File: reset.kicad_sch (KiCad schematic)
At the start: 12 parts

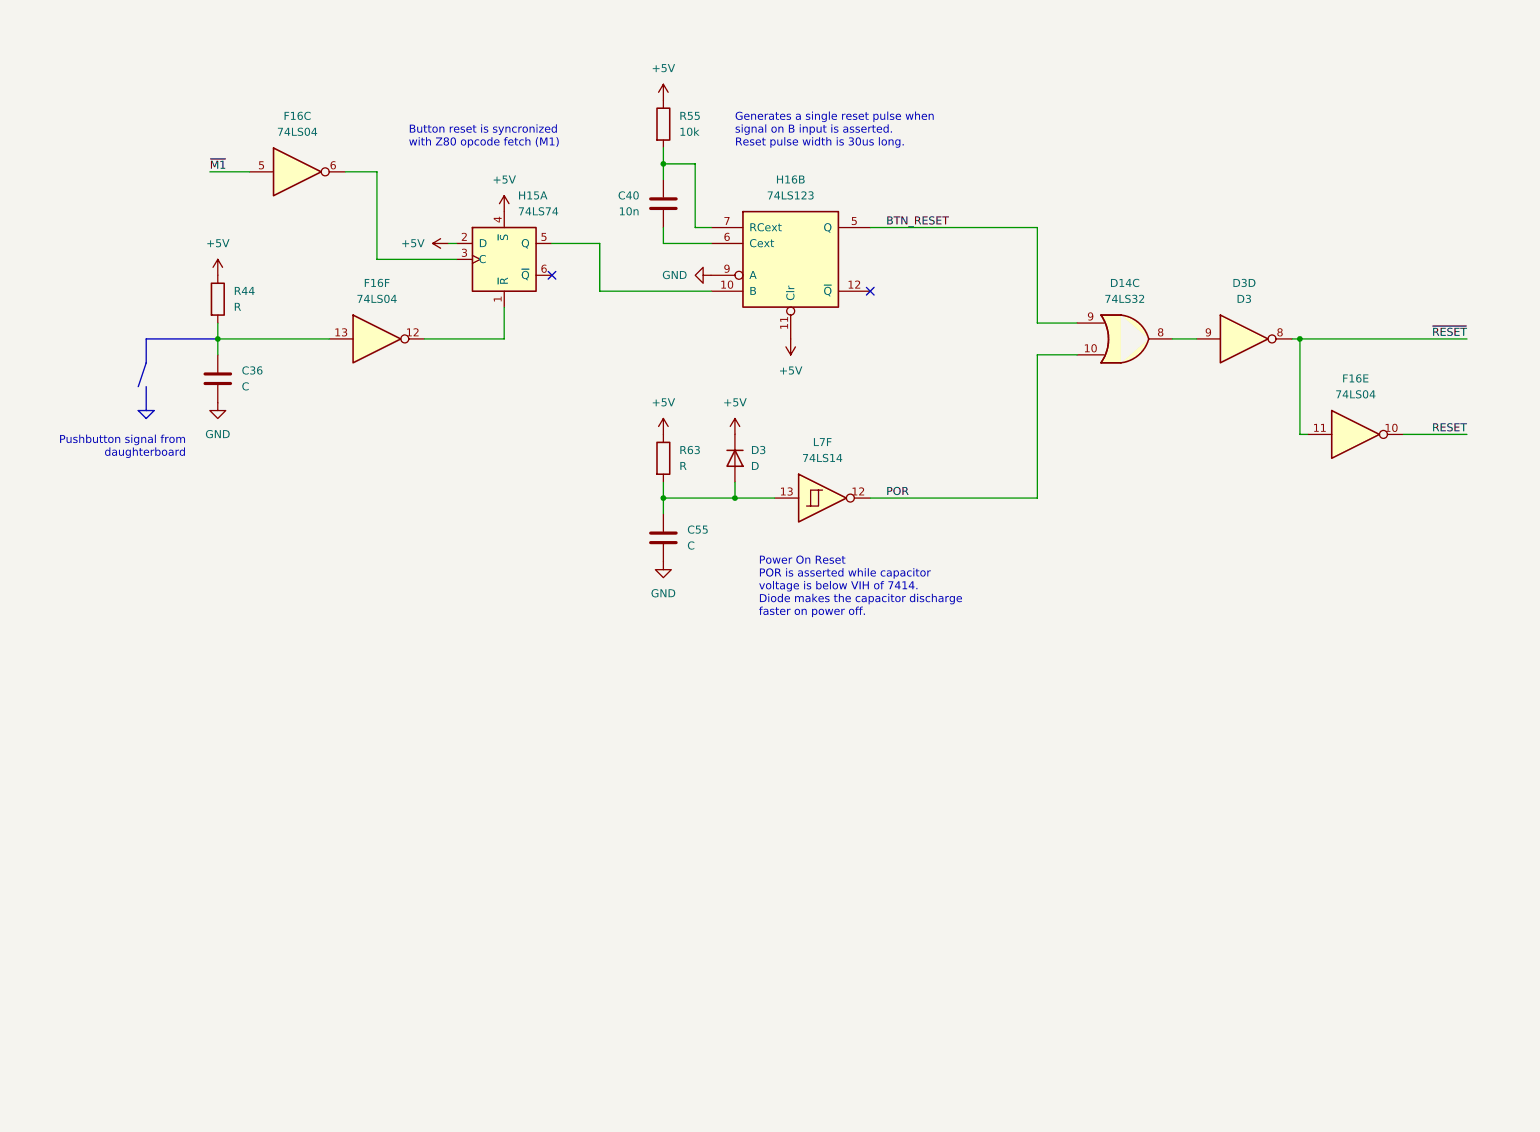
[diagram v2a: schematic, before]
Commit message: Moved clock circuit in the clock/reset sheet
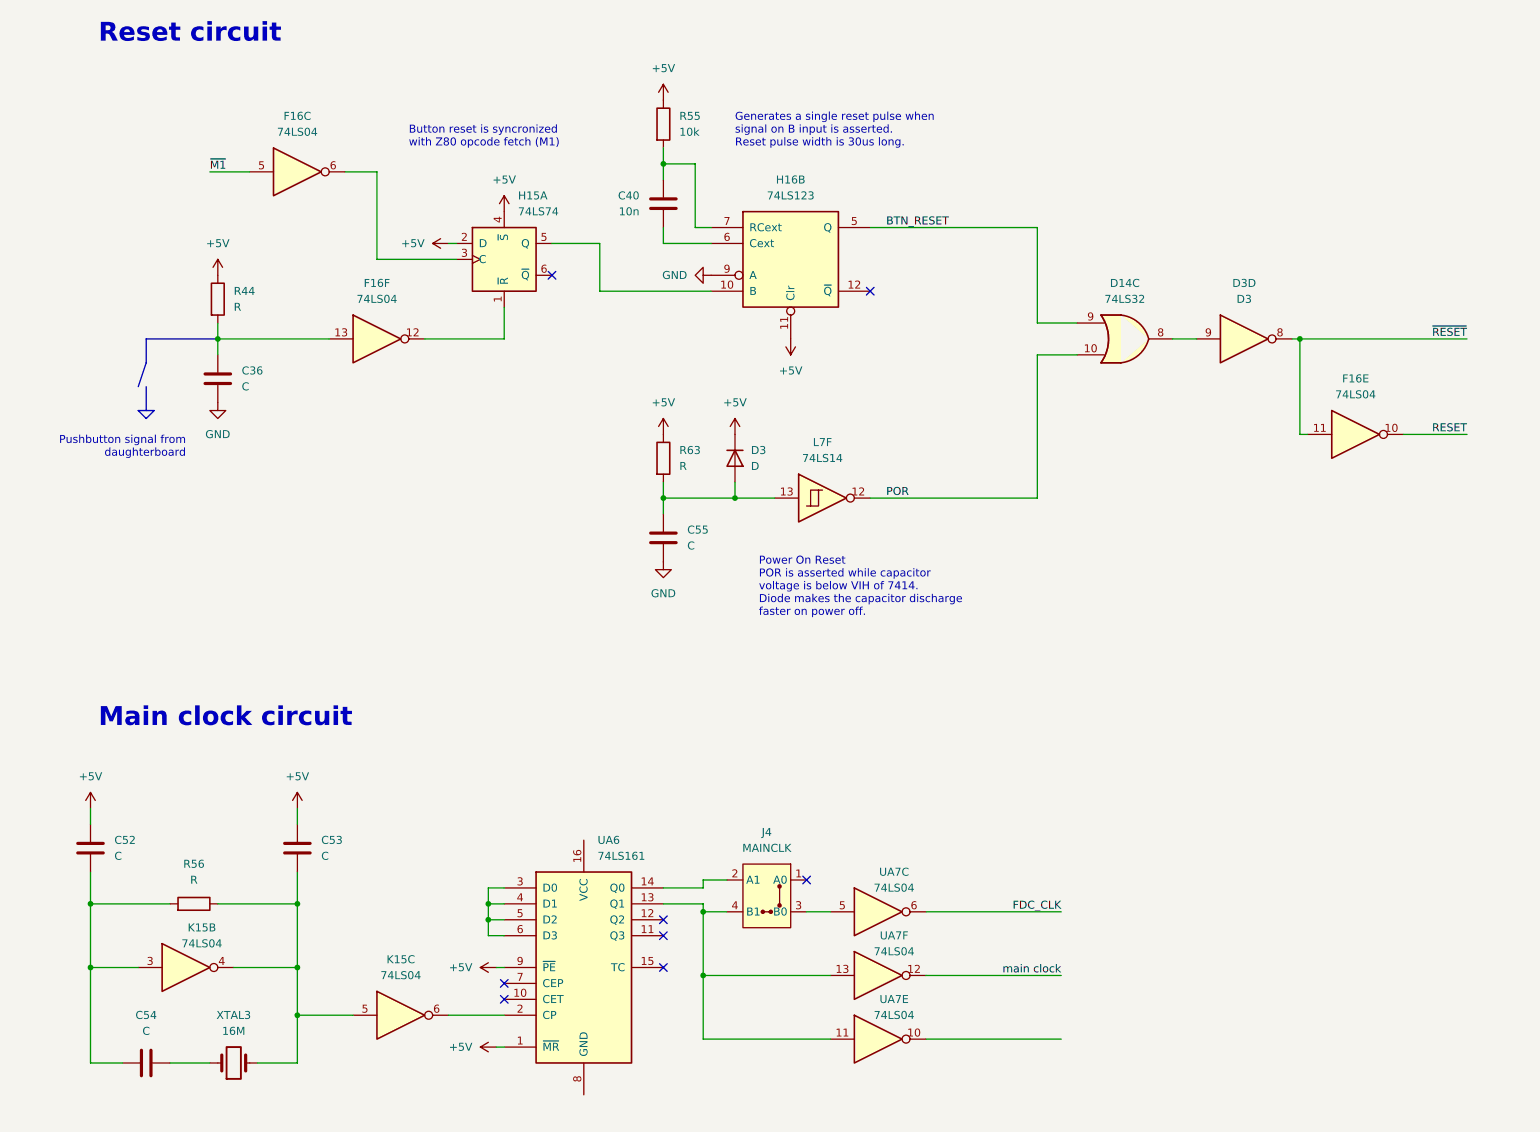
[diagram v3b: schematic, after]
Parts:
- added C52, C53, C54: C, symbol Device:C
- added J4: MAINCLK, symbol ceda:MAINCLK
- added K15, UA7: 74LS04, symbol 74xx:74LS04
- added R56: R, symbol Device:R
- added UA6: 74LS161, symbol 74xx:74LS161
- added XTAL3: 16M, symbol Device:Crystal
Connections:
- net +5V: now also C52.2, C53.2, UA6.1 (~{MR}), UA6.9 (~{PE})
- new net: J4.4 (B1), UA6.13 (Q1), UA7.11, UA7.13
- new net: J4.2 (A1), UA6.14 (Q0)
- new net: K15.6, UA6.2 (CP)
- new net: UA6.3 (D0), UA6.4 (D1), UA6.5 (D2), UA6.6 (D3)
- new net: C52.1, C54.2, K15.3, R56.2
- new net: J4.3 (B0), UA7.5
- new net: C54.1, XTAL3.1
- new net: C53.1, K15.4, K15.5, R56.1, XTAL3.2
- new net FDC_CLK: UA7.6
- new net main clock: UA7.12
- no-connect marks 2 -> 8
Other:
- note added: "Main clock circuit"
- note added: "Reset circuit"

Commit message: Z80 and reset/clock: wire naming
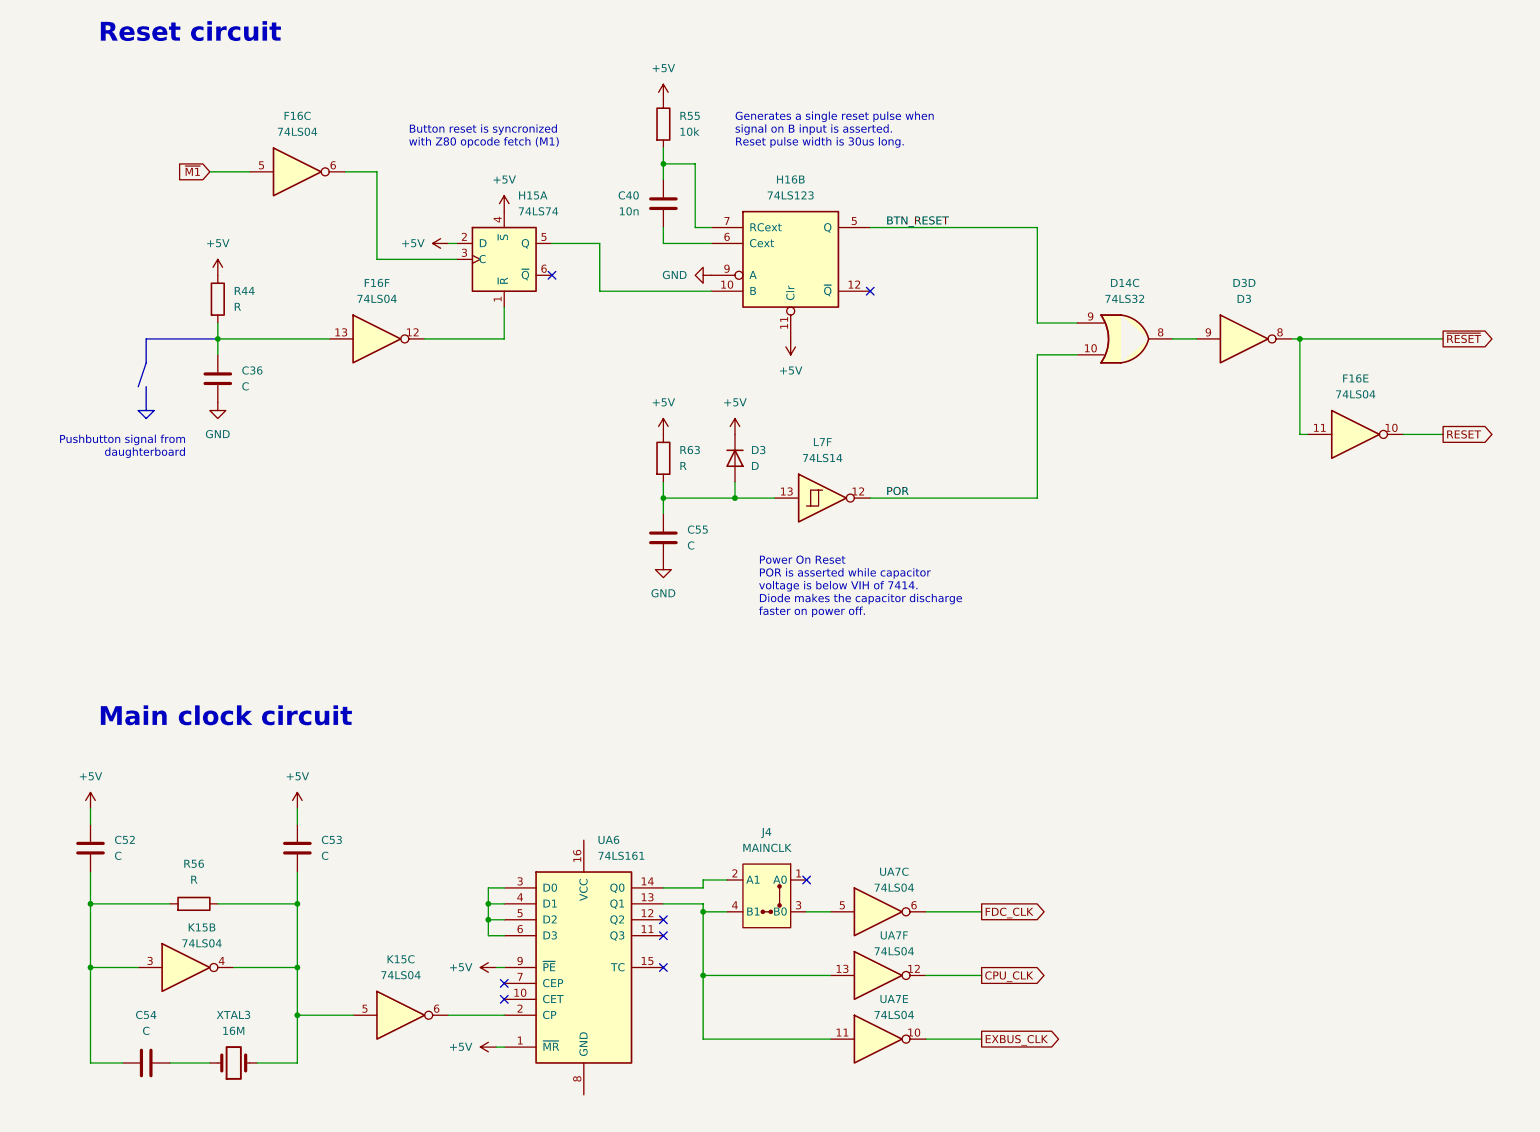
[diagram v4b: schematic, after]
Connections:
- net EXBUS_CLK: now reaches UA7.10
- net main clock renamed CPU_CLK
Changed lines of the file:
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@@
     (stroke (width 0) (type default))
   )
-  (wire (pts (xy 153.67 173.99) (xy 175.26 173.99))
+  (wire (pts (xy 153.67 173.99) (xy 162.56 173.99))
     (stroke (width 0) (type default))
   )
@@
     (stroke (width 0) (type default))
   )
-  (wire (pts (xy 213.36 72.39) (xy 240.03 72.39))
+  (wire (pts (xy 213.36 72.39) (xy 236.22 72.39))
     (stroke (width 0) (type default))
   )
@@
     (stroke (width 0) (type default))
   )
-  (wire (pts (xy 153.67 184.15) (xy 175.26 184.15))
+  (wire (pts (xy 153.67 184.15) (xy 162.56 184.15))
     (stroke (width 0) (type default))
   )
@@
     (stroke (width 0) (type default))
   )
-  (wire (pts (xy 229.87 87.63) (xy 240.03 87.63))
+  (wire (pts (xy 229.87 87.63) (xy 236.22 87.63))
     (stroke (width 0) (type default))
   )
@@
     (stroke (width 0) (type default))
   )
-  (wire (pts (xy 175.26 163.83) (xy 153.67 163.83))
+  (wire (pts (xy 162.56 163.83) (xy 153.67 163.83))
     (stroke (width 0) (type default))
   )
@@
     (effects (font (size 3 3) (thickness 1) bold) (justify left bottom))
   )
-  (label "RESET" (at 240.03 87.63 180) (fields_autoplaced)
-    (effects (font (size 1.27 1.27)) (justify right bottom))
-  )
   (label "BTN_RESET" (at 147.32 54.61 0) (fields_autoplaced)
     (effects (font (size 1.27 1.27)) (justify left bottom))
   )
-  (label "~{RESET}" (at 240.03 72.39 180) (fields_autoplaced)
-    (effects (font (size 1.27 1.27)) (justify right bottom))
-  )
-  (label "~{M1}" (at 39.37 45.72 0) (fields_autoplaced)
-    (effects (font (size 1.27 1.27)) (justify left bottom))
-  )
   (label "POR" (at 147.32 97.79 0) (fields_autoplaced)
     (effects (font (size 1.27 1.27)) (justify left bottom))
   )
-  (label "FDC_CLK" (at 175.26 163.83 180) (fields_autoplaced)
-    (effects (font (size 1.27 1.27)) (justify right bottom))
-  )
-  (label "main clock" (at 175.26 173.99 180) (fields_autoplaced)
-    (effects (font (size 1.27 1.27)) (justify right bottom))
+  (global_label "RESET" (shape output) (at 236.22 87.63 0) (fields_autoplaced)
+    (effects (font (size 1.27 1.27)) (justify left))
+    (property "Intersheetrefs" "${INTERSHEET_REFS}" (at 244.9503 87.63 0)
+      (effects (font (size 1.27 1.27)) (justify left) hide)
+    )
+  )
+  (global_label "CPU_CLK" (shape output) (at 162.56 173.99 0) (fields_autoplaced)
+    (effects (font (size 1.27 1.27)) (justify left))
+    (property "Intersheetrefs" "${INTERSHEET_REFS}" (at 173.9514 173.99 0)
+      (effects (font (size 1.27 1.27)) (justify left) hide)
+    )
+  )
+  (global_label "~{M1}" (shape input) (at 39.37 45.72 180) (fields_autoplaced)
+    (effects (font (size 1.27 1.27)) (justify right))
+    (property "Intersheetrefs" "${INTERSHEET_REFS}" (at 33.7239 45.72 0)
+      (effects (font (size 1.27 1.27)) (justify right) hide)
+    )
+  )
+  (global_label "FDC_CLK" (shape output) (at 162.56 163.83 0) (fields_autoplaced)
+    (effects (font (size 1.27 1.27)) (justify left))
+    (property "Intersheetrefs" "${INTERSHEET_REFS}" (at 173.7095 163.83 0)
+      (effects (font (size 1.27 1.27)) (justify left) hide)
+    )
+  )
+  (global_label "EXBUS_CLK" (shape output) (at 162.56 184.15 0) (fields_autoplaced)
+    (effects (font (size 1.27 1.27)) (justify left))
+    (property "Intersheetrefs" "${INTERSHEET_REFS}" (at 176.2494 184.15 0)
+      (effects (font (size 1.27 1.27)) (justify left) hide)
+    )
+  )
+  (global_label "~{RESET}" (shape output) (at 236.22 72.39 0) (fields_autoplaced)
+    (effects (font (size 1.27 1.27)) (justify left))
+    (property "Intersheetrefs" "${INTERSHEET_REFS}" (at 244.9503 72.39 0)
+      (effects (font (size 1.27 1.27)) (justify left) hide)
+    )
   )
   (symbol (lib_id "74xx:74LS14") (at 137.16 97.79 0) (unit 6)

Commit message: Daughterboard
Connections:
- net ~{RESET_BTN}: now reaches C36.1, F16.13, R44.2
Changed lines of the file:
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@@
+    (stroke (width 0) (type default))
+  )
+  (wire (pts (xy 29.21 72.39) (xy 40.64 72.39))
     (stroke (width 0) (type default))
   )
@@
     (stroke (width 0) (type default))
   )
-  (polyline (pts (xy 40.64 72.39) (xy 29.21 72.39))
-    (stroke (width 0) (type default))
-  )
   (polyline (pts (xy 29.21 85.09) (xy 30.48 83.82))
     (stroke (width 0) (type default))
@@
     (effects (font (size 1.27 1.27)) (justify left bottom))
   )
+  (label "~{RESET_BTN}" (at 29.21 72.39 0) (fields_autoplaced)
+    (effects (font (size 1.27 1.27)) (justify left bottom))
+  )
